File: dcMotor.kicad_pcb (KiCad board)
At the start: 2 copper layers, 144.9 x 98 mm, 136 parts, among them J1 USB_C_Receptacle_USB2.0_16P, J3 Conn_ST_STDC14, J6 Conn_01x02_Pin, J7 Conn_01x04_Pin, J8 Conn_01x06_Pin, Q1 AO3400A, SW1 SW_Push, SW2 SW_Push, U1 LMR54406DBVR, U10 MCP6561-OT, U11 TLV9152IDR, U12 NUCLEO-F411RE:NUCLEO-F411RE, U13 INA241B4IDR, U2 NCP718ASNADJT1G, U3 NCP718ASNADJT1G, U5 TLV9152IDR, U6 ER_OLEDM0.91_1x-I2C, U7 STM32G431CBTx, U8 LTH-301-05, U9 DRV8231ADDA

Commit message: finished
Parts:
- added C47: 22µF, Capacitor_SMD:C_1206_3216Metric_Pad1.33x1.80mm_HandSolder, F.Cu at (70.5, 73.5)
- added C48: 22µF, Capacitor_SMD:C_1206_3216Metric_Pad1.33x1.80mm_HandSolder, F.Cu at (74.7, 73.5)
- moved TP17 83.0 mm to (185.5, 75.2)
- moved C44 54.7 mm to (57.6, 66.4), turned to 90 degrees
- moved TP14 27.3 mm to (104.8, 86.4)
- moved R37 10.3 mm to (62.7, 86.6), turned to -90 degrees
- moved R18 4.26 mm to (95.7, 76.3)
- moved R35 4.26 mm to (99.5, 76.3)
- moved U11 4.22 mm to (100.1, 71.2)
- moved R33 4.22 mm to (95.6, 73.4)
- moved R34 4.22 mm to (95.6, 71.3)
- moved C41 4.07 mm to (96.9, 68.8), turned to -90 degrees
- moved JP3 3.43 mm to (54.2, 67.5), turned to 0 degrees
- moved R38 0.38 mm to (64.8, 86.6)
- moved C28 0.13 mm to (53.9, 73.7)
- moved C43 0.13 mm to (62.3, 79.6)
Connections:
- R35 pad 1: /MOTOR-SENSE -> /UMOTOR
- TP6 pad 1: /IPROPI -> /IMOTOR
- U11 pad 1: /MOTOR-SENSE -> /UMOTOR
- U11 pad 5: unconnected-(U11B-+-Pad5) -> +1.65V
- U11 pad 6: unconnected-(U11B---Pad6) -> Net-(U11B--)
- U11 pad 7: unconnected-(U11-Pad7) -> Net-(U11B--)
- U7 pad 25: /IMOTOR -> /UMOTOR
- U7 pad 26: /VBUS_SENSE -> /IMOTOR
- U7 pad 29: unconnected-(U7-PB15-Pad29) -> /VBUS_SENSE
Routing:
- net /UMOTOR: track 0.00 -> 66.0 mm, vias 0 -> 6
- net +1.65V: track 51.0 -> 71.9 mm, vias 2 -> 4
- net /HALL_B: track 72.8 -> 88.8 mm
- net +3.3V: track 321.9 -> 337.2 mm, vias 9 -> 11
- net /HALL_A: track 82.9 -> 97.9 mm
- net VBUS: track 132.5 -> 142.3 mm, vias 6 -> 2
- net GND: track 213.8 -> 223.4 mm, vias 137 -> 145
- net Net-(U9-IN1): track 22.4 -> 31.5 mm, vias 0 -> 2
- net Net-(U11A-+): track 0.00 -> 8.85 mm
- net Net-(U11A--): track 0.00 -> 6.54 mm
- net /MOTOR-_SENSE: track 85.3 -> 91.5 mm
- net /ISHUNT: track 23.4 -> 28.2 mm
- net Net-(JP2-C): track 48.1 -> 52.3 mm
- net /TIM1_CH1: track 178.9 -> 175.0 mm
- net /IMOTOR: track 186.9 -> 184.3 mm
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
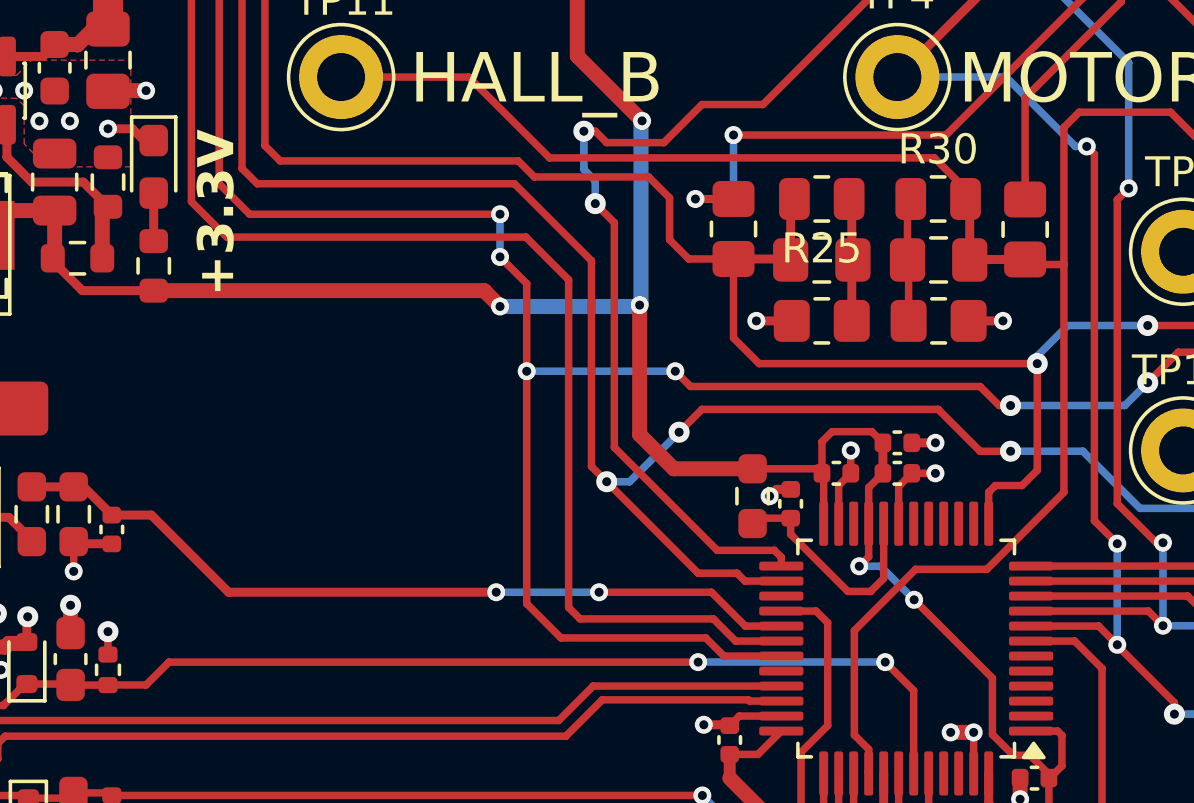
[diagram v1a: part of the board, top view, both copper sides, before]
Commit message: have to change pins towards Nucleo and add jumpers
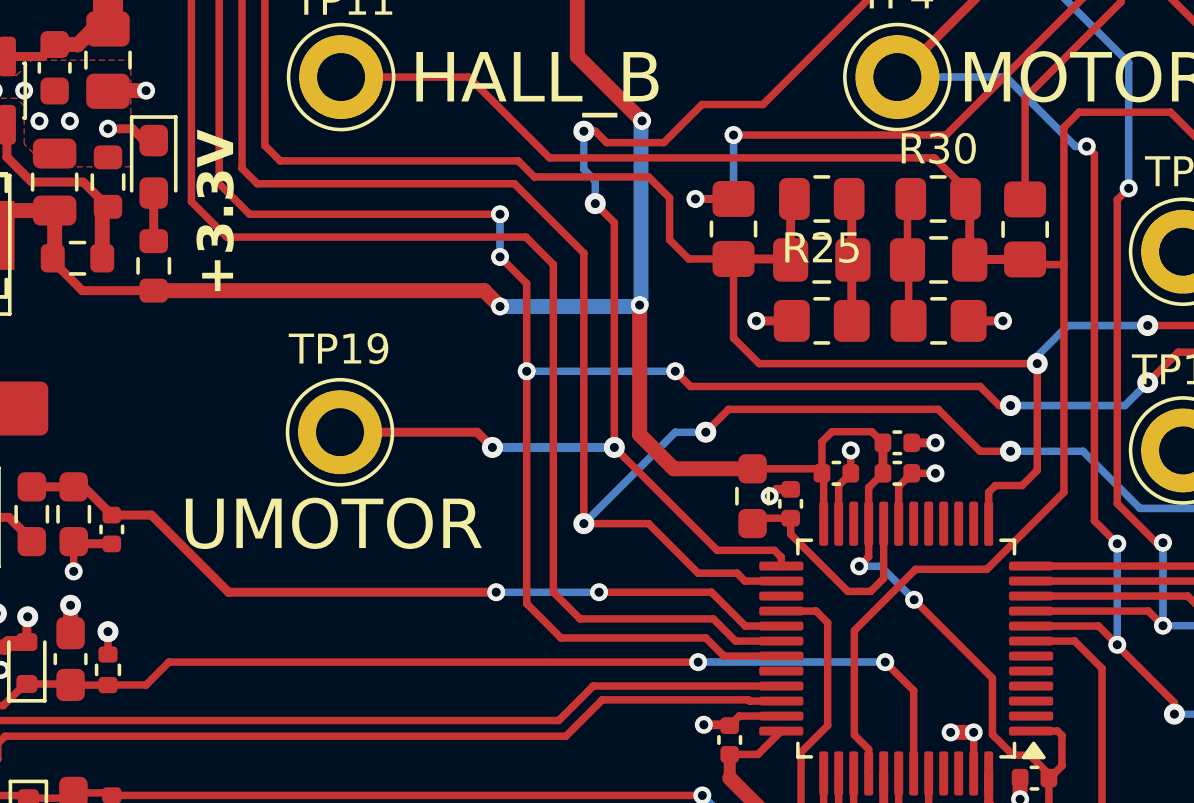
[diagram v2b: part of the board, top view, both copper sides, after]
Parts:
- added TP19: TP_Keystone_5095, PZ:TP_Keystone_5010-5014_Multipurpose, F.Cu at (67.7, 114.0)
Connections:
- U12 pad CN10_23: unconnected-(U12B-PA8-PadCN10_23) -> /TIM2_CH1
- U12 pad CN10_25: unconnected-(U12B-PB10-PadCN10_25) -> /TIM2_CH2
- U12 pad CN10_27: /EN_PHOTO -> /BUTTON1
- U12 pad CN10_29: /BUTTON1 -> /TIM1_CH2
- U12 pad CN10_31: unconnected-(U12B-PB3-PadCN10_31) -> /TIM1_CH1
- U12 pad CN10_35: /MOTOR+_SENSE -> unconnected-(U12B-PA2-PadCN10_35)
- U12 pad CN10_37: /MOTOR-_SENSE -> unconnected-(U12B-PA3-PadCN10_37)
- U12 pad CN7_28: /TIM1_CH1 -> /MOTOR-_SENSE
- U12 pad CN7_30: /TIM1_CH2 -> /MOTOR+_SENSE
- U12 pad CN7_32: /TIM2_CH2 -> /EN_PHOTO
- U12 pad CN7_34: /TIM2_CH1 -> /POT
- U12 pad CN7_38: /POT -> /UMOTOR
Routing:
- net /UMOTOR: track 66.0 -> 75.3 mm, vias 6 -> 8
- net /IMOTOR: track 184.3 -> 186.9 mm
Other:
- board text added: "UMOTOR"

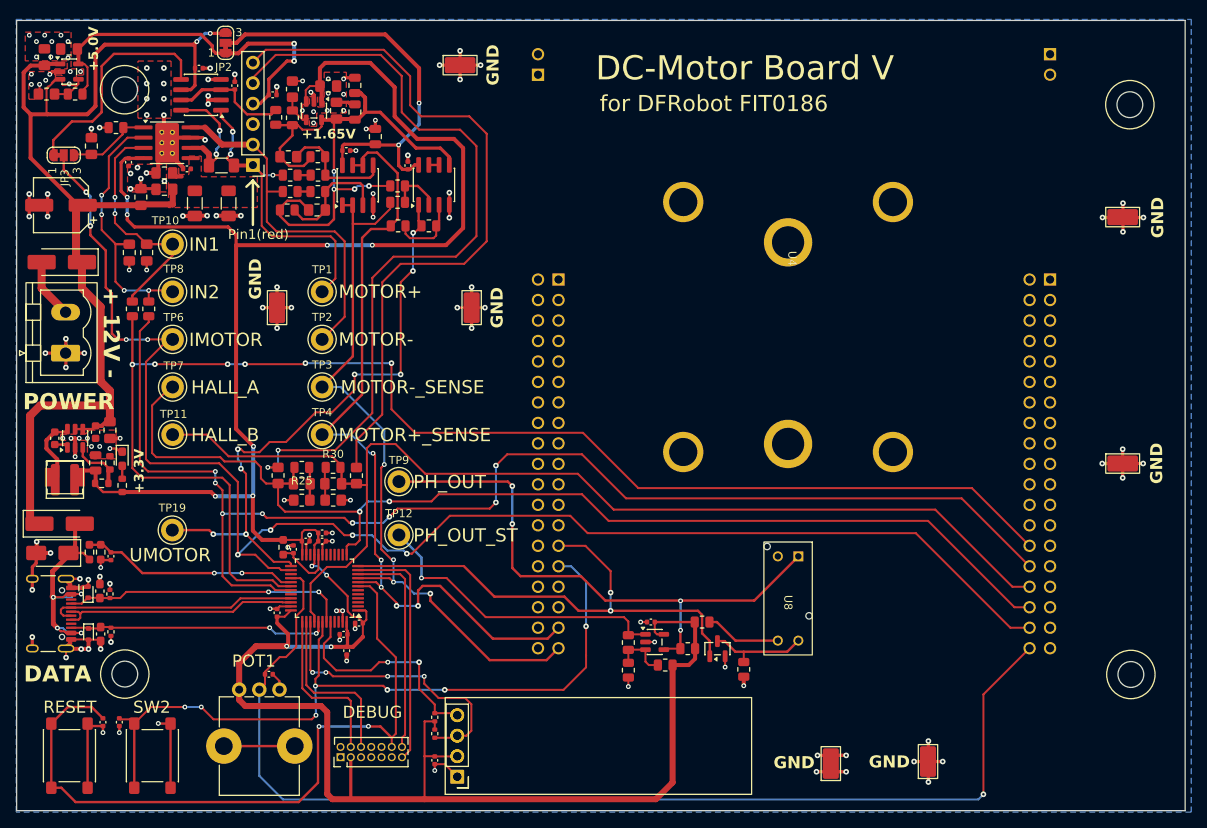
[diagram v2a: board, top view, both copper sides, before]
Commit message: nucleo supplied with VIN = 12V
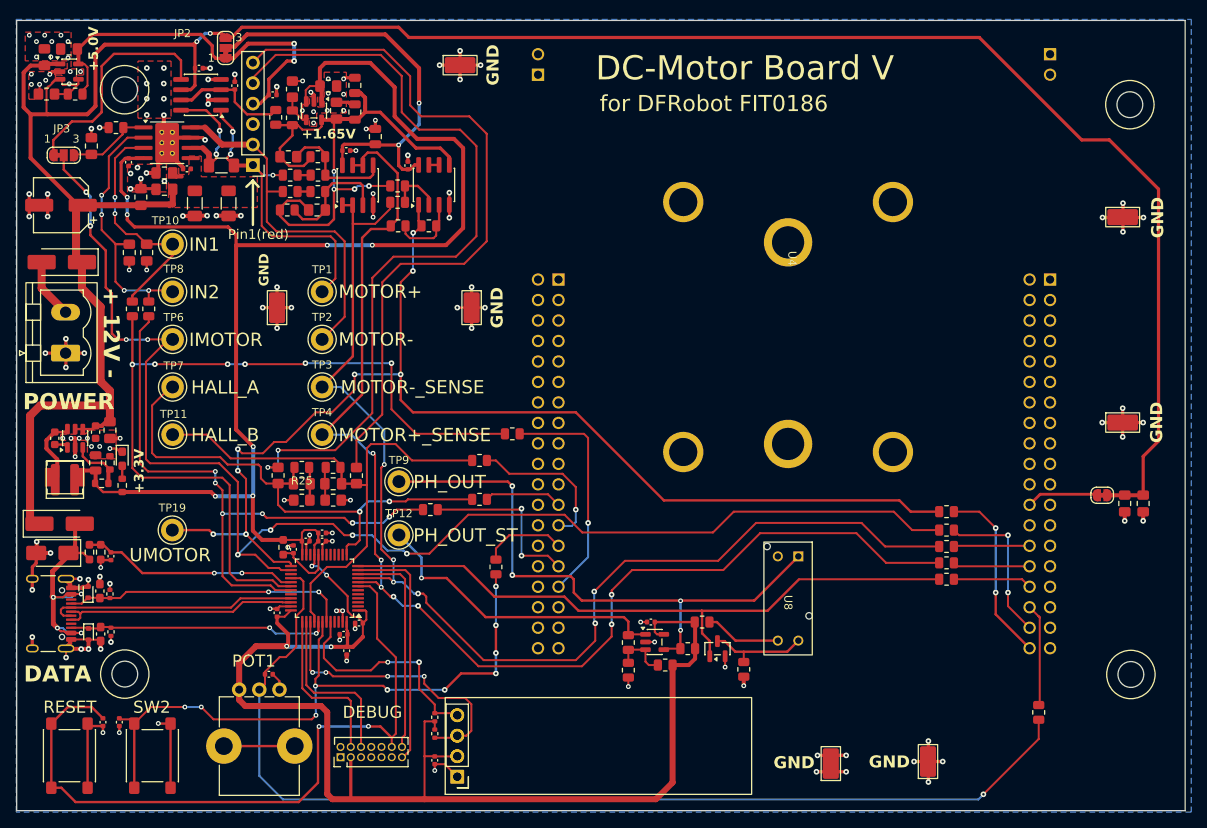
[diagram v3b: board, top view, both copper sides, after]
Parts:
- added C36: 1u, Capacitor_SMD:C_0805_2012Metric_Pad1.18x1.45mm_HandSolder, F.Cu at (188.1, 110.7)
- added C49: 1u, Capacitor_SMD:C_0805_2012Metric_Pad1.18x1.45mm_HandSolder, F.Cu at (185.8, 110.7)
- added JP4: SolderJumper_2_Bridged, Jumper:SolderJumper-2_P1.3mm_Bridged_RoundedPad1.0x1.5mm, F.Cu at (183.0, 109.7)
- added R39: 0, Resistor_SMD:R_0805_2012Metric, F.Cu at (105.8, 110.2)
- added R41: 0, Resistor_SMD:R_0805_2012Metric, F.Cu at (105.8, 105.4)
- added R44: 0, Resistor_SMD:R_0805_2012Metric, F.Cu at (107.8, 118.6)
- added R45: 0, Resistor_SMD:R_0805_2012Metric, F.Cu at (99.7, 111.5)
- added R46: 0, Resistor_SMD:R_0805_2012Metric, F.Cu at (109.8, 102.1)
- added R47: 0, Resistor_SMD:R_0805_2012Metric, F.Cu at (163.7, 114.0)
- added R48: 0, Resistor_SMD:R_0805_2012Metric, F.Cu at (163.7, 111.7)
- added R49: 0, Resistor_SMD:R_0805_2012Metric, F.Cu at (175.1, 136.6)
- added R50: 0, Resistor_SMD:R_0805_2012Metric, F.Cu at (163.7, 120.1)
- added R51: 0, Resistor_SMD:R_0805_2012Metric, F.Cu at (163.7, 118.1)
- added R52: 0, Resistor_SMD:R_0805_2012Metric, F.Cu at (163.7, 116.0)
- moved TP16 5.08 mm to (185.5, 100.7)
- moved JP2 0.63 mm to (74.3, 54.2)
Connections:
- U12 pad CN10_23: /TIM2_CH1 -> Net-(U12B-PA8)
- U12 pad CN10_25: /TIM2_CH2 -> Net-(U12B-PB10)
- U12 pad CN10_27: /BUTTON1 -> Net-(U12B-PB4)
- U12 pad CN10_29: /TIM1_CH2 -> Net-(U12B-PB5)
- U12 pad CN10_31: /TIM1_CH1 -> Net-(U12B-PB3)
- U12 pad CN7_24: unconnected-(U12A-VIN-PadCN7_24) -> Net-(JP4-B)
- U12 pad CN7_28: /MOTOR-_SENSE -> Net-(U12A-PA0)
- U12 pad CN7_30: /MOTOR+_SENSE -> Net-(U12A-PA1)
- U12 pad CN7_32: /EN_PHOTO -> Net-(U12A-PA4)
- U12 pad CN7_34: /POT -> Net-(U12A-PB0)
- U12 pad CN7_36: /IMOTOR -> Net-(U12A-PC1)
- U12 pad CN7_38: /UMOTOR -> Net-(U12A-PC0)
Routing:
- net VBUS: track 142.3 -> 309.4 mm
- net /TIM1_CH2: track 163.6 -> 77.1 mm, vias 8 -> 6
- net /UMOTOR: track 75.3 -> 151.1 mm
- net /TIM2_CH2: track 143.9 -> 68.3 mm
- net /TIM2_CH1: track 140.7 -> 65.5 mm
- net /TIM1_CH1: track 175.0 -> 104.2 mm
- net /MOTOR-_SENSE: track 91.5 -> 150.0 mm, vias 4 -> 6
- net /MOTOR+_SENSE: track 101.4 -> 157.8 mm, vias 5 -> 7
- net Net-(U12B-PB3): track 0.00 -> 28.7 mm, vias 0 -> 1
- net Net-(U12A-PC0): track 0.00 -> 22.7 mm, vias 0 -> 2
- net Net-(U12B-PB5): track 0.00 -> 21.4 mm, vias 0 -> 2
- net Net-(U12A-PC1): track 0.00 -> 19.7 mm, vias 0 -> 2
- net Net-(U12B-PB10): track 0.00 -> 19.1 mm, vias 0 -> 1
- net /EN_PHOTO: track 63.5 -> 82.1 mm, vias 2 -> 0
- net /BUTTON1: track 96.3 -> 82.2 mm, vias 7 -> 10
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
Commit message: minor modifications
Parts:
- moved C33 0.48 mm to (80.6, 60.0)
- moved J8 0.19 mm to (77.9, 68.7)
- moved R40 0.18 mm to (73.6, 68.9)
- moved R42 0.09 mm to (80.6, 62.9)
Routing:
- net +5.0V: track 48.0 -> 45.2 mm
- net GND: track 225.6 -> 223.7 mm, vias 147 -> 146
- net /HALL_A: track 97.9 -> 97.4 mm

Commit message: minor modifications
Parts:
- added J2: Conn_01x02_Socket, Connector_PinSocket_2.54mm:PinSocket_1x02_P2.54mm_Vertical, F.Cu at (146.8, 135.8)
- added J4: Conn_01x02_Socket, Connector_PinSocket_2.54mm:PinSocket_1x02_P2.54mm_Vertical, F.Cu at (150.9, 133.3)
- moved SW1 0.51 mm to (54.9, 142.5)
- moved SW2 0.51 mm to (65.2, 142.5)
- moved C24 0.51 mm to (59.1, 138.3)
- moved C26 0.51 mm to (61.1, 138.3)
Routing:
- net /PHOTO_OUT: track 74.2 -> 93.0 mm, vias 4 -> 5
- net Net-(J2-Pin_1): track 9.44 -> 25.4 mm
- net Net-(J2-Pin_2): track 12.5 -> 18.7 mm
- net /IMOTOR: track 172.9 -> 170.3 mm
- net /HALL_B: track 88.6 -> 87.7 mm

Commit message: latest updates
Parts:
- U13: value INA241B4IDR -> INA241A4IDR

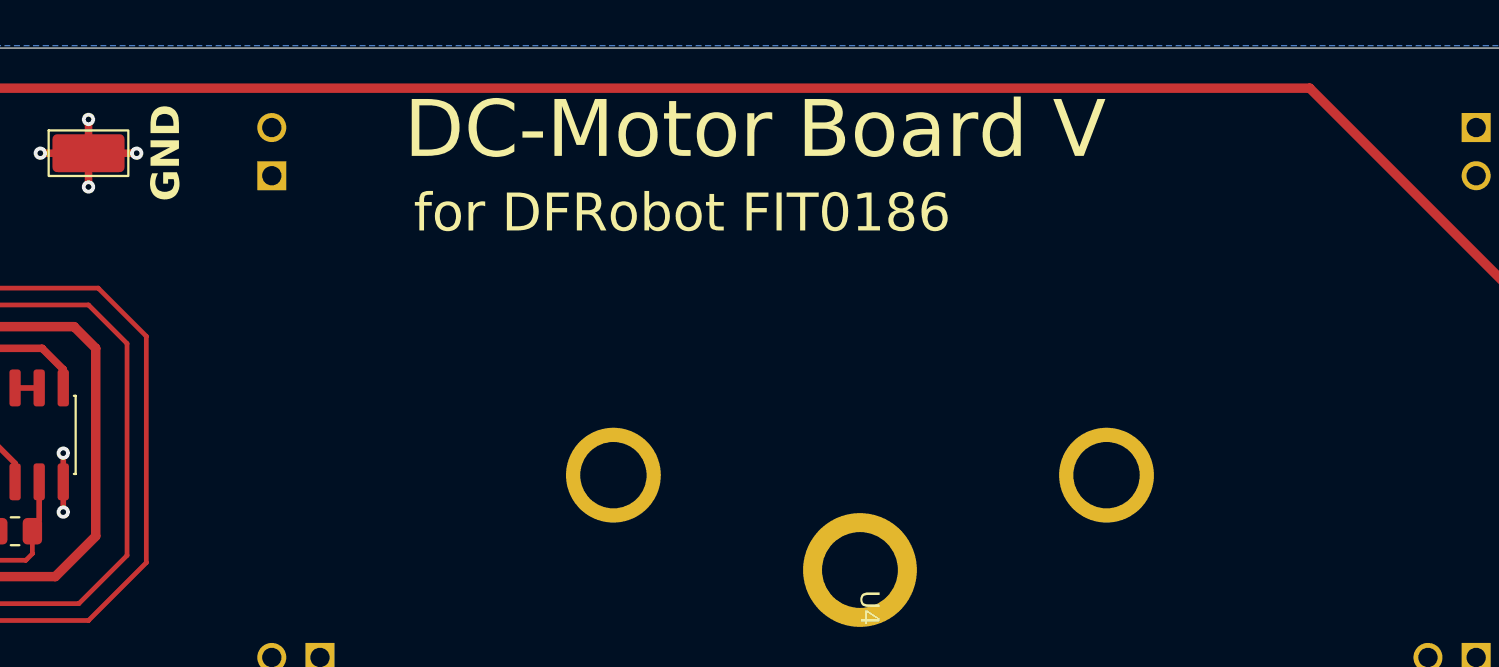
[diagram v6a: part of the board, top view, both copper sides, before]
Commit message: corrected rotation of U9, still bom makes seom troubles at JLC
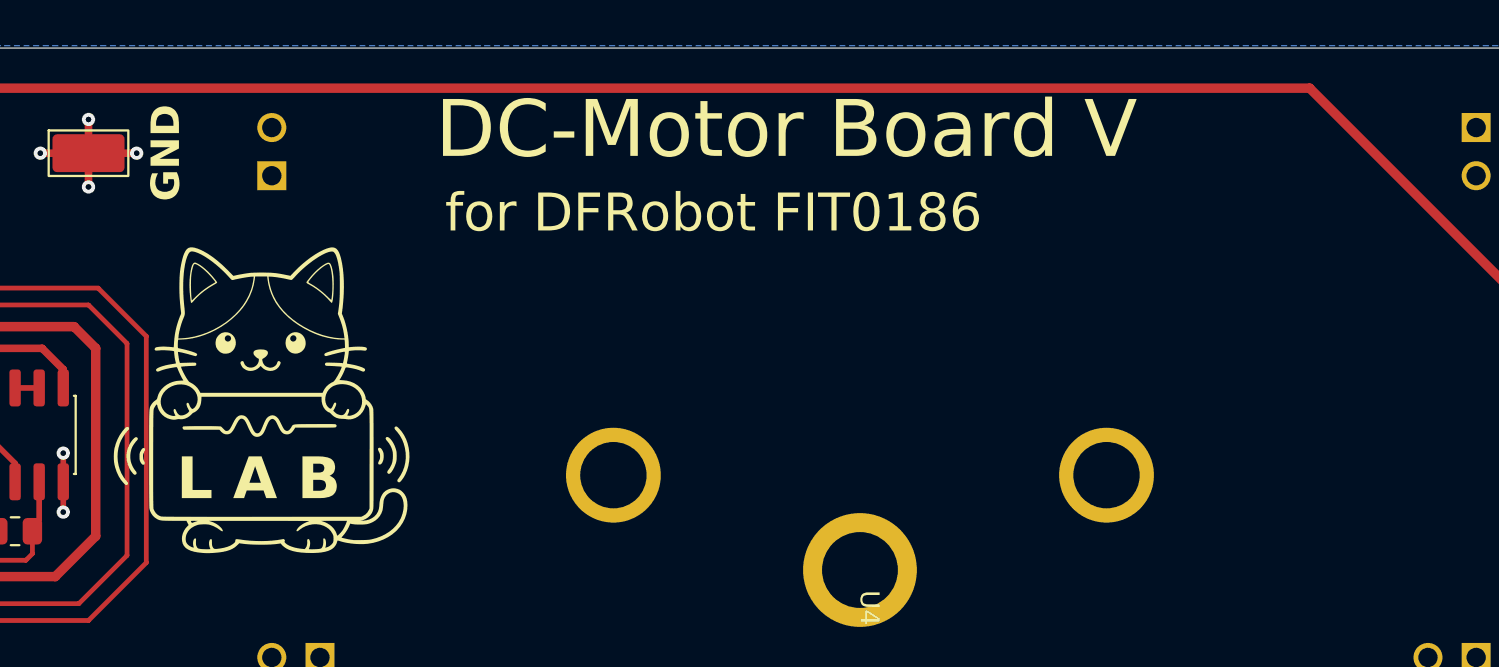
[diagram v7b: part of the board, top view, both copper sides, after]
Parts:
- added G***: LOGO, LOGO, F.Cu at (112.5, 69.3)
- U9: value DRV8231ADDA -> DRV8251ADDA

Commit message: minor mods
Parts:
- added R27: 10k, Resistor_SMD:R_0805_2012Metric, F.Cu at (93.5, 126.7)
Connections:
- U7 pad 45: unconnected-(U7-PB8-Pad45) -> /BOOT0
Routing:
- net /BOOT0: track 0.00 -> 13.2 mm
- net GND: track 223.7 -> 224.8 mm, vias 146 -> 147
